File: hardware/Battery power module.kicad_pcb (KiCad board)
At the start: 2 copper layers, 20 x 26 mm, 17 parts, among them J1 USB_C_Receptacle_PowerOnly_6P, J2 Conn_01x02, U1 BQ24090DGQ

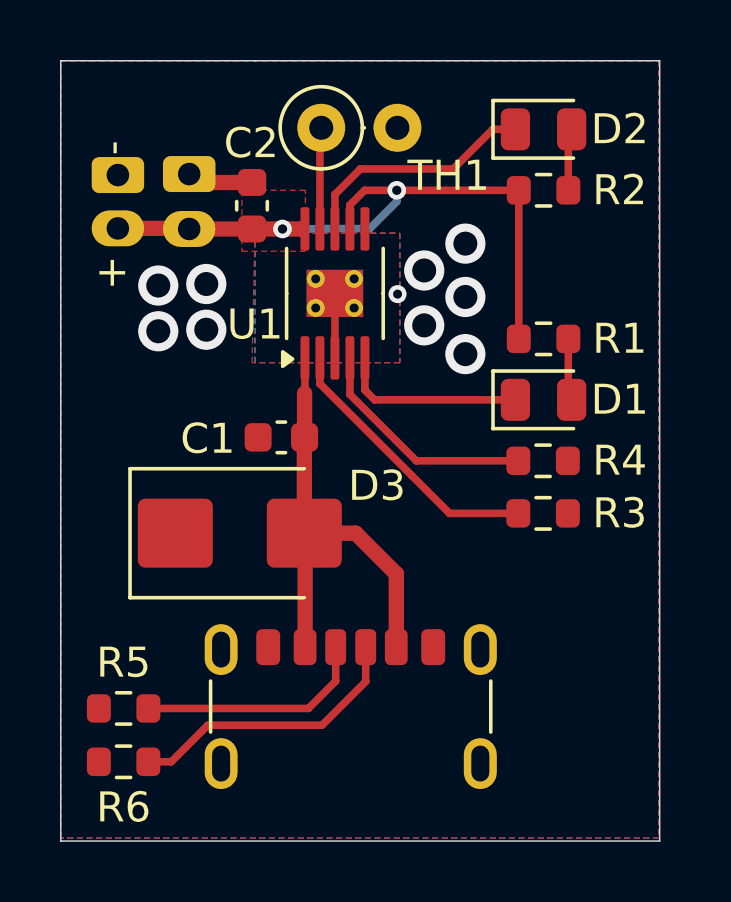
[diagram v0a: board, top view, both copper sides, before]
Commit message: Version 1.1: Extending the USB port beyond the board outline and adding a version designation on the PCB
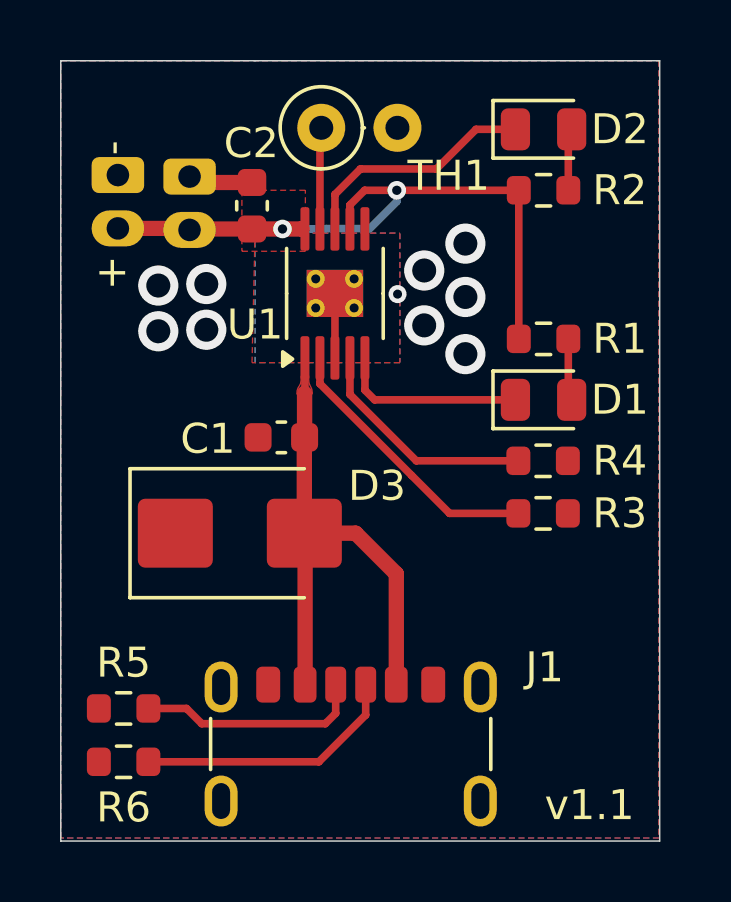
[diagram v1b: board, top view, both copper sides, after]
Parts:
- removed J2: Conn_01x02, Connector_JST:JST_PH_B2B-PH-K_1x02_P2.00mm_Vertical
- added ?: , , F.Cu at (124.3, 97.8)
- added ?: , , F.Cu at (124.3, 99.6)
- moved J1 1.25 mm to (129.7, 117.9)
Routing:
- net /VBUS: track 15.8 -> 18.3 mm
- added copper zone on F.Cu, net /CC2
- added copper zone on F.Cu, net /CHG
- added copper zone on F.Cu, net /VBUS
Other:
- board text added: "v1.1"
